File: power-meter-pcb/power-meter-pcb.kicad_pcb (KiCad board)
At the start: 2 copper layers, 3 parts, among them J1 USB4105-GF-A, U1 ESP32-S3-WROOM-1, U2 TPD3E001DRLR

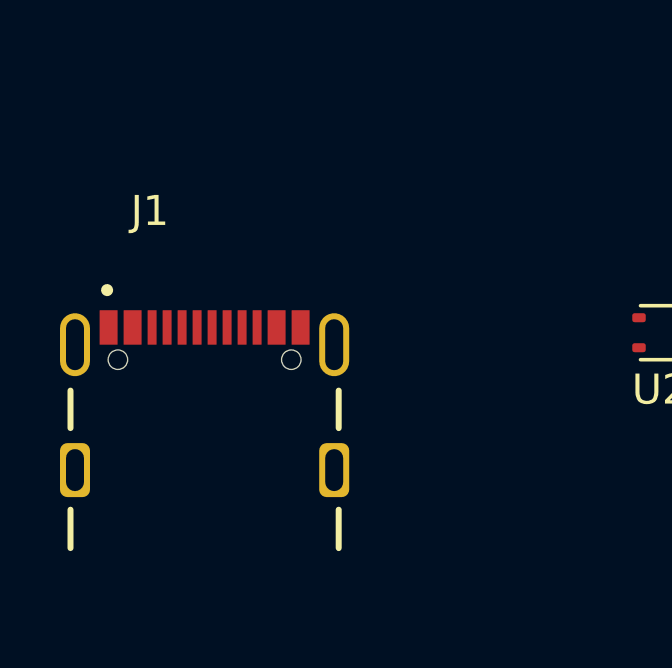
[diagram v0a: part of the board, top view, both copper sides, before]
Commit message: Added amplifier, IMU, inter board connections
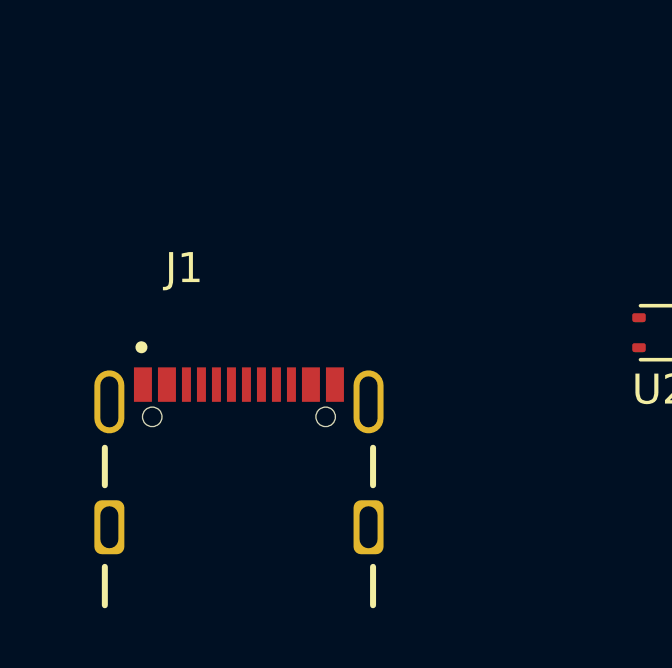
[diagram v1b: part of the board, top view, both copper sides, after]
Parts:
- moved J1 2.22 mm to (118.7, 105.4)
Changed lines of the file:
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@@
 		)
 		(fp_text user "${REFERENCE}"
-			(at 0 0 270)
+			(at 0 0 -90)
 			(layer "F.Fab")
 			(effects
@@
 	(footprint "USB4105:GCT_USB4105-GF-A"
 		(layer "F.Cu")
-		(at 117.6 103.505)
+		(at 118.745 105.41)
 		(property "Reference" "J1"
 			(at -1.825 -8.635 0)

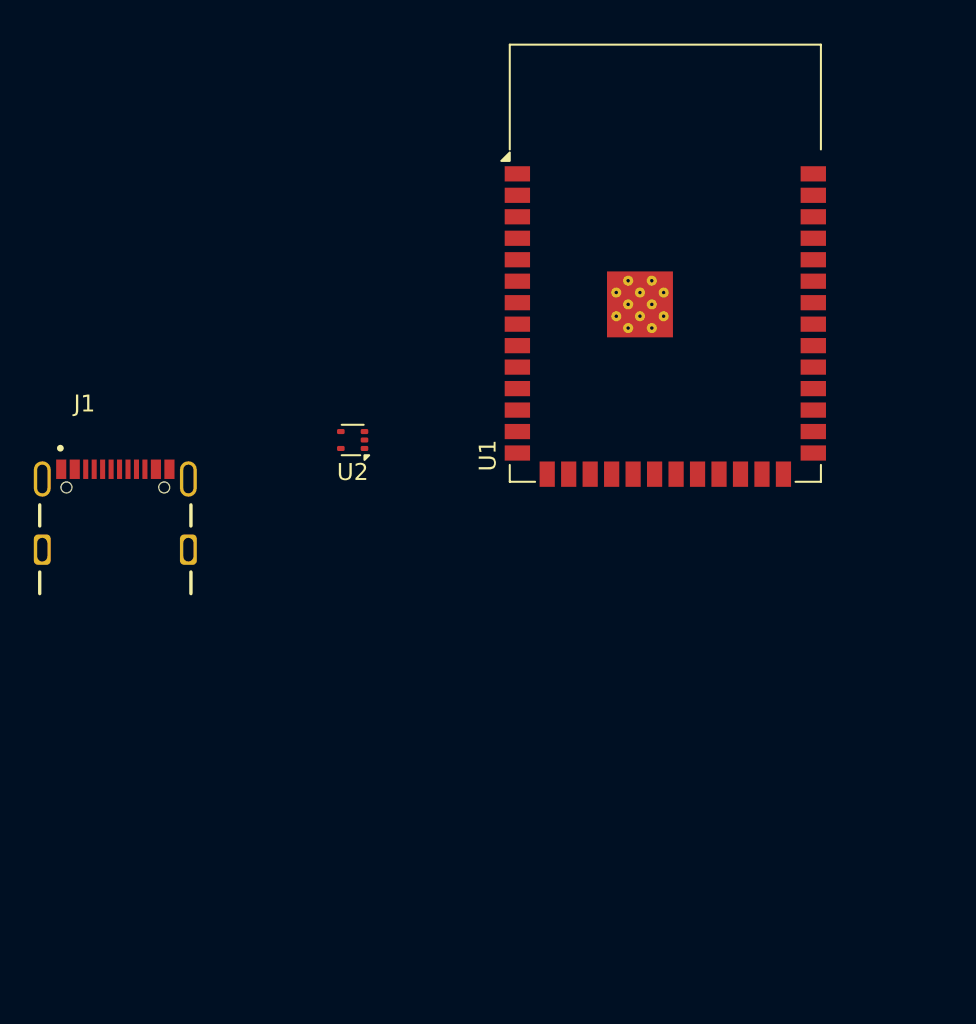
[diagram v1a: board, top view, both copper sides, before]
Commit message: Assigning footprints, extremely rough idea of size
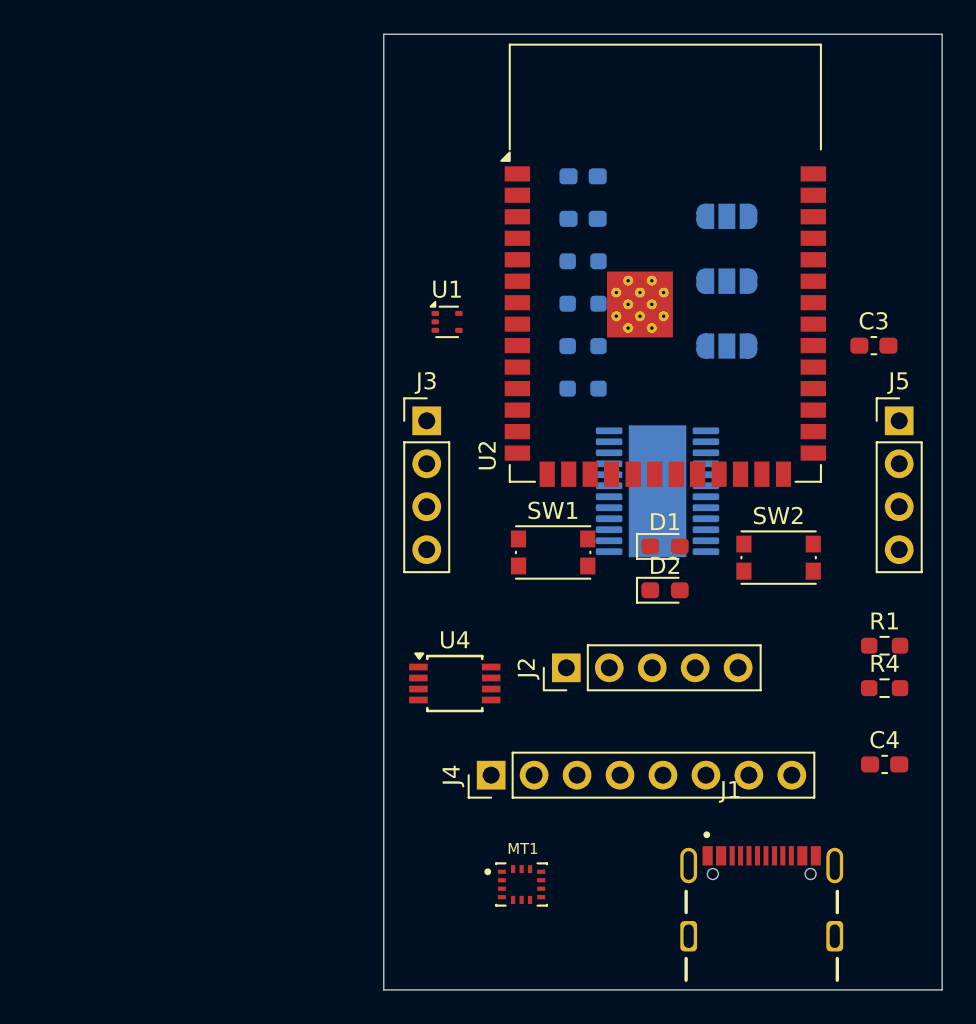
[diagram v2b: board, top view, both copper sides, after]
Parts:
- removed the U2 at (132.8, 98.9)
- added C1: 1u, Capacitor_SMD:C_0603_1608Metric_Pad1.08x0.95mm_HandSolder, B.Cu at (146.4, 83.3)
- added C2: 1u, Capacitor_SMD:C_0603_1608Metric_Pad1.08x0.95mm_HandSolder, B.Cu at (146.4, 85.8)
- added C3: C, Capacitor_SMD:C_0603_1608Metric_Pad1.08x0.95mm_HandSolder, F.Cu at (163.6, 93.3)
- added C4: 100n, Capacitor_SMD:C_0603_1608Metric_Pad1.08x0.95mm_HandSolder, F.Cu at (164.2, 118.1)
- added D1: LED, LED_SMD:LED_0603_1608Metric_Pad1.05x0.95mm_HandSolder, F.Cu at (151.3, 105.2)
- added D2: LED, LED_SMD:LED_0603_1608Metric_Pad1.05x0.95mm_HandSolder, F.Cu at (151.3, 107.8)
- added J2: Debug, Connector_PinHeader_2.54mm:PinHeader_1x05_P2.54mm_Vertical, F.Cu at (145.4, 112.4)
- added J3: Side A, Connector_PinHeader_2.54mm:PinHeader_1x04_P2.54mm_Vertical, F.Cu at (137.2, 97.8)
- added J4: Crank interconnect, Connector_PinHeader_2.54mm:PinHeader_1x08_P2.54mm_Vertical, F.Cu at (141.0, 118.7)
- added J5: Side B, Connector_PinHeader_2.54mm:PinHeader_1x04_P2.54mm_Vertical, F.Cu at (165.1, 97.8)
- added JP1: Address select, Jumper:SolderJumper-3_P1.3mm_Open_RoundedPad1.0x1.5mm, B.Cu at (154.9, 85.7)
- added JP2: Amp select, Jumper:SolderJumper-3_P1.3mm_Open_RoundedPad1.0x1.5mm, B.Cu at (154.9, 89.5)
- added JP3: Amp select, Jumper:SolderJumper-3_P1.3mm_Open_RoundedPad1.0x1.5mm, B.Cu at (154.9, 93.4)
- added MT1: ICM-42670-P, ICM-42670-P_AccelGyro:XDCR_ICM-42670-P, F.Cu at (142.8, 125.2)
- added R1: 5.1k, Resistor_SMD:R_0603_1608Metric_Pad0.98x0.95mm_HandSolder, F.Cu at (164.2, 111.1)
- added R2: 10k, Resistor_SMD:R_0603_1608Metric_Pad0.98x0.95mm_HandSolder, B.Cu at (146.4, 88.4)
- added R3: 10k, Resistor_SMD:R_0603_1608Metric_Pad0.98x0.95mm_HandSolder, B.Cu at (146.4, 90.9)
- added R4: 5.1k, Resistor_SMD:R_0603_1608Metric_Pad0.98x0.95mm_HandSolder, F.Cu at (164.2, 113.6)
- added R5: 150, Resistor_SMD:R_0603_1608Metric_Pad0.98x0.95mm_HandSolder, B.Cu at (146.4, 93.4)
- added R6: 150, Resistor_SMD:R_0603_1608Metric_Pad0.98x0.95mm_HandSolder, B.Cu at (146.4, 95.9)
- added SW1: EN, Button_Switch_SMD:SW_Push_1P1T_NO_CK_KMR2, F.Cu at (144.6, 105.6)
- added SW2: BOOT, Button_Switch_SMD:SW_Push_1P1T_NO_CK_KMR2, F.Cu at (158.0, 105.9)
- added U1: TPD3E001DRLR, Package_TO_SOT_SMD:SOT-553, F.Cu at (138.4, 91.9)
- added U3: ADS1232IPW, Package_SO:HTSSOP-24-1EP_4.4x7.8mm_P0.65mm_EP3.4x7.8mm_Mask2.4x4.68mm, B.Cu at (150.8, 102.0)
- added U4: P3T1755, Package_SO:TSSOP-8_3x3mm_P0.65mm, F.Cu at (138.8, 113.3)
- moved J1 44.5 mm to (157.0, 128.3)
- renumbered U1 to U2
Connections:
- net /DN renamed /USB and charging/USB.DN
- net /DP renamed /USB and charging/USB.DP
- J1 pad A1_B12: GND1 -> GNDD
- J1 pad B1_A12: GND1 -> GNDD
- J1 pad SH1: GND1 -> GNDD
- J1 pad SH2: GND1 -> GNDD
- J1 pad SH3: GND1 -> GNDD
- J1 pad SH4: GND1 -> GNDD
- U2 pad 1: Net-(U1-GND-Pad1) -> GNDD
- U2 pad 15: unconnected-(U1-IO3-Pad15) -> /Accelerometer/SPI.SDO
- U2 pad 16: unconnected-(U1-IO46-Pad16) -> /AMP_PWDN
- U2 pad 2: unconnected-(U1-3V3-Pad2) -> +3.3V
- U2 pad 24: unconnected-(U1-IO47-Pad24) -> /AMP2.DOUT
- U2 pad 25: unconnected-(U1-IO48-Pad25) -> /AMP2.SCLK
- U2 pad 26: unconnected-(U1-IO45-Pad26) -> /AMP1.SCLK
- U2 pad 27: unconnected-(U1-IO0-Pad27) -> /BOOT
- U2 pad 31: unconnected-(U1-IO38-Pad31) -> /LED1
- U2 pad 32: unconnected-(U1-IO39-Pad32) -> /LED2
- U2 pad 35: unconnected-(U1-IO42-Pad35) -> /AMP1.DOUT
- U2 pad 36: unconnected-(U1-RXD0-Pad36) -> /UART.RX
- U2 pad 37: unconnected-(U1-TXD0-Pad37) -> /UART.TX
- U2 pad 38: unconnected-(U1-IO2-Pad38) -> /Accelerometer/SPI.SCLK
- U2 pad 39: unconnected-(U1-IO1-Pad39) -> /Accelerometer/SPI.AC_CS
- U2 pad 4: unconnected-(U1-IO4-Pad4) -> /Accelerometer/SPI.SDI
- U2 pad 40: Net-(U1-GND-Pad1) -> GNDD
- U2 pad 41: Net-(U1-GND-Pad1) -> GNDD
- U2 pad 5: unconnected-(U1-IO5-Pad5) -> /Accelerometer/Interrupt
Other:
- board outline added: 33 x 56.5 mm

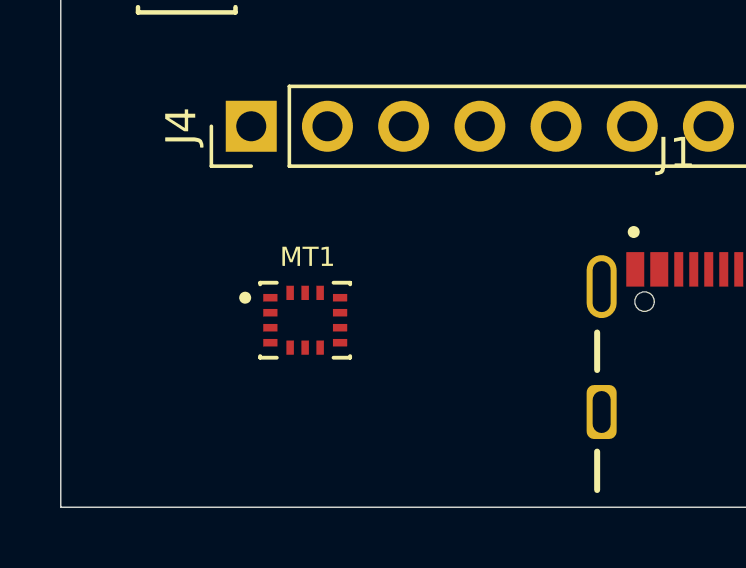
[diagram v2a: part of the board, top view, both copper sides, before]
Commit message: Added power supply to PCB
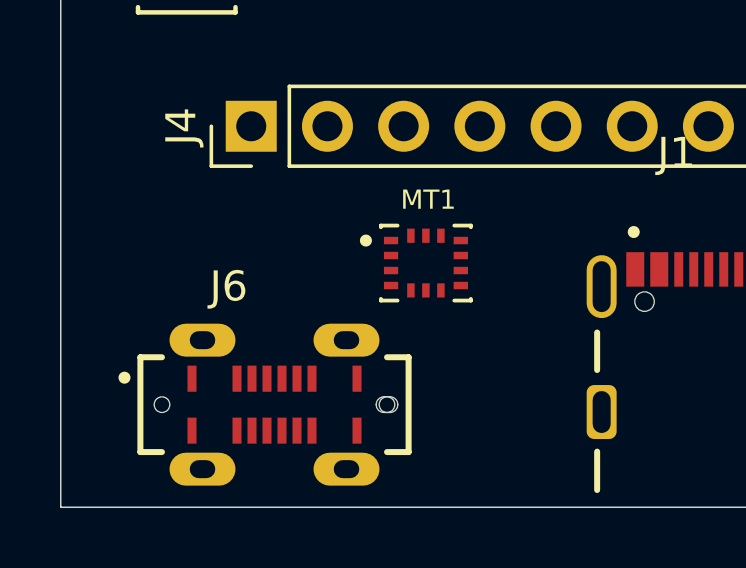
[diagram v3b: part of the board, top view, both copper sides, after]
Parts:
- added J6: USB4120-03-C_REVA, USB4120:GCT_USB4120-03-C_REVA, F.Cu at (141.7, 128.0)
- moved MT1 4.45 mm to (146.8, 123.3)
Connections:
- U4 pad 1: (no net) -> /I2C.SCL
- U4 pad 2: (no net) -> /I2C.SDA
- U4 pad 3: (no net) -> unconnected-(U4-ALERT-Pad3)
- U4 pad 4: (no net) -> GNDD
- U4 pad 5: (no net) -> GNDD
- U4 pad 6: (no net) -> GNDD
- U4 pad 7: (no net) -> Net-(JP1-C)
- U4 pad 8: (no net) -> +3.3V

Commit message: Started PCB layout
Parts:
- removed the J1 at (157.0, 128.3)
- removed the R1 at (164.2, 111.1)
- removed the R4 at (164.2, 113.6)
- added BT1: Battery_Cell, Connector_JST:JST_EH_B2B-EH-A_1x02_P2.50mm_Vertical, F.Cu at (110.5, 127.0)
- added C10: 10u, Capacitor_SMD:C_0603_1608Metric_Pad1.08x0.95mm_HandSolder, F.Cu at (109.4, 94.6)
- added C12: 0.1u, Capacitor_SMD:C_0603_1608Metric_Pad1.08x0.95mm_HandSolder, B.Cu at (138.2, 69.4)
- added C13: 0.1u, Capacitor_SMD:C_0603_1608Metric_Pad1.08x0.95mm_HandSolder, B.Cu at (128.5, 72.4)
- added C15: 0.1u, Capacitor_SMD:C_0603_1608Metric_Pad1.08x0.95mm_HandSolder, F.Cu at (112.1, 76.7)
- added C3: 10u, Capacitor_SMD:C_0603_1608Metric_Pad1.08x0.95mm_HandSolder, F.Cu at (105.1, 89.6)
- added C4: 10u, Capacitor_SMD:C_0603_1608Metric_Pad1.08x0.95mm_HandSolder, F.Cu at (105.1, 92.1)
- added C5: 0.1u, Capacitor_SMD:C_0603_1608Metric_Pad1.08x0.95mm_HandSolder, F.Cu at (105.1, 94.6)
- added C6: 10u, Capacitor_SMD:C_0603_1608Metric_Pad1.08x0.95mm_HandSolder, F.Cu at (105.1, 97.1)
- added C7: 0.1u, Capacitor_SMD:C_0603_1608Metric_Pad1.08x0.95mm_HandSolder, F.Cu at (105.1, 99.6)
- added C8: 10u, Capacitor_SMD:C_0603_1608Metric_Pad1.08x0.95mm_HandSolder, F.Cu at (109.4, 89.6)
- added C9: 10u, Capacitor_SMD:C_0603_1608Metric_Pad1.08x0.95mm_HandSolder, F.Cu at (109.4, 92.1)
- added D3: LED, LED_SMD:LED_0603_1608Metric_Pad1.05x0.95mm_HandSolder, F.Cu at (115.5, 102.2)
- added FB1: MH2029-300Y, Inductor_SMD:L_0805_2012Metric, F.Cu at (110.3, 106.6)
- added L1: 4.7uH, Inductor_SMD:L_Murata_DFE201610P, F.Cu at (115.1, 105.1)
- added NT1: NetTie_2, NetTie:NetTie-2_SMD_Pad0.5mm, B.Cu at (133.1, 70.0)
- added NT3: NetTie_2, NetTie:NetTie-2_SMD_Pad0.5mm, B.Cu at (136.7, 60.0)
- added Q1: AS2302, Package_TO_SOT_SMD:TSOT-23, F.Cu at (118.6, 90.8)
- added Q2: AS2302, Package_TO_SOT_SMD:TSOT-23, F.Cu at (116.9, 121.0)
- added Q3: AS2302, Package_TO_SOT_SMD:TSOT-23, B.Cu at (140.8, 67.2)
- added R10: 470, Resistor_SMD:R_0603_1608Metric_Pad0.98x0.95mm_HandSolder, F.Cu at (113.8, 97.1)
- added R11: 1M, Resistor_SMD:R_0603_1608Metric_Pad0.98x0.95mm_HandSolder, F.Cu at (115.1, 73.7)
- added R12: 1M, Resistor_SMD:R_0603_1608Metric_Pad0.98x0.95mm_HandSolder, F.Cu at (121.8, 79.2)
- added R13: 47, Resistor_SMD:R_0603_1608Metric_Pad0.98x0.95mm_HandSolder, B.Cu at (139.1, 75.1)
- added R14: 47, Resistor_SMD:R_0603_1608Metric_Pad0.98x0.95mm_HandSolder, B.Cu at (139.1, 73.6)
- added R15: 47, Resistor_SMD:R_0603_1608Metric_Pad0.98x0.95mm_HandSolder, B.Cu at (139.1, 72.1)
- added R5: 5.1k, Resistor_SMD:R_0603_1608Metric_Pad0.98x0.95mm_HandSolder, F.Cu at (109.4, 97.1)
- added R6: 2.2k, Resistor_SMD:R_0603_1608Metric_Pad0.98x0.95mm_HandSolder, F.Cu at (109.4, 99.6)
- added R7: 470, Resistor_SMD:R_0603_1608Metric_Pad0.98x0.95mm_HandSolder, F.Cu at (113.8, 89.6)
- added R8: 5.1k, Resistor_SMD:R_0603_1608Metric_Pad0.98x0.95mm_HandSolder, F.Cu at (113.8, 92.1)
- added R9: 2k, Resistor_SMD:R_0603_1608Metric_Pad0.98x0.95mm_HandSolder, F.Cu at (113.8, 94.6)
- added U3: MCP73831-2-OT, Package_TO_SOT_SMD:SOT-23-5, F.Cu at (105.5, 103.3)
- added U5: S-8261AAJMD-G2JT2U, Package_TO_SOT_SMD:SOT-23-6, F.Cu at (105.5, 107.9)
- added U6: TPS63031DSK, Package_SON:WSON-10-1EP_2.5x2.5mm_P0.5mm_EP1.2x2mm, F.Cu at (123.2, 103.2)
- C1, C2: moved to F.Cu
- C11: renamed from C3; value C -> 0.1u; moved to B.Cu
- C14: renamed from C4; value 100n -> 0.1u
- J4: renamed from J3; moved to B.Cu
- J5: moved to B.Cu
- JP3: renamed from JP1; moved to F.Cu
- R1: renamed from R2; moved to F.Cu
- R2: renamed from R3; moved to F.Cu
- R3: renamed from R5; moved to F.Cu
- R4: renamed from R6; moved to F.Cu
- U7: renamed from U3; footprint Package_SO:HTSSOP-24-1EP_4.4x7.8mm_P0.65mm_EP3.4x7.8mm_Mask2.4x4.68mm -> Package_SO:TSSOP-24_4.4x7.8mm_P0.65mm
- moved MT1 47.3 mm to (155.0, 76.7)
- moved C11 44.0 mm to (128.5, 66.8), turned to 90 degrees
- moved J5 42.7 mm to (147.3, 58.9), turned to 180 degrees
- moved J4 41.3 mm to (123.2, 58.9), turned to 180 degrees
- moved U7 36.8 mm to (133.3, 69.6), turned to 0 degrees
- moved J2 36.1 mm to (129.0, 80.2)
- moved U1 36.1 mm to (135.3, 56.1)
- moved JP3 36.0 mm to (170.7, 53.3), turned to 90 degrees
- moved JP2 24.5 mm to (143.8, 71.5), turned to 90 degrees
- moved JP1 17.1 mm to (143.8, 76.6), turned to 90 degrees
- moved R2 9.35 mm to (155.6, 88.9), turned to 0 degrees
- moved R3 7.63 mm to (154.0, 93.0), turned to 0 degrees
- moved R4 7.59 mm to (153.8, 97.5), turned to 0 degrees
- moved R1 6.13 mm to (146.4, 94.5), turned to 0 degrees
- moved C2 4.60 mm to (146.8, 90.4), turned to 0 degrees
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- renumbered J4 to J1, J6 to J3, JP2 to JP1, JP3 to JP2, U2 to U1, U4 to U2, U1 to U4
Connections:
- net Net-(J3-Pin_2) renamed /Strain gauge amplifier/GA
- net Net-(J3-Pin_3) renamed /Strain gauge amplifier/GB
- J3 pad A1: unconnected-(J6-GND_A-PadA1) -> GNDD
- J3 pad A12: unconnected-(J6-GND_A__1-PadA12) -> GNDD
- J3 pad A4: unconnected-(J6-VBUS_A-PadA4) -> +5V
- J3 pad A5: unconnected-(J6-CC1-PadA5) -> Net-(J3-CC1)
- J3 pad A6: unconnected-(J6-D1+-PadA6) -> /USB and charging/USB.DP
- J3 pad A7: unconnected-(J6-D1--PadA7) -> /USB and charging/USB.DN
- J3 pad A9: unconnected-(J6-VBUS_A__1-PadA9) -> +5V
- J3 pad B1: unconnected-(J6-GND_B-PadB1) -> GNDD
- J3 pad B12: unconnected-(J6-GND_B__1-PadB12) -> GNDD
- J3 pad B4: unconnected-(J6-VBUS_B-PadB4) -> +5V
- J3 pad B5: unconnected-(J6-CC2-PadB5) -> Net-(J3-CC2)
- J3 pad B6: unconnected-(J6-D2+-PadB6) -> /USB and charging/USB.DN
- J3 pad B7: unconnected-(J6-D2--PadB7) -> /USB and charging/USB.DP
- J3 pad B9: unconnected-(J6-VBUS_B__1-PadB9) -> +5V
- J3 pad S1: unconnected-(J6-SHIELD-PadS1) -> GNDD
- J3 pad S2: unconnected-(J6-SHIELD__1-PadS2) -> GNDD
- J3 pad S3: unconnected-(J6-SHIELD__2-PadS3) -> GNDD
- J3 pad S4: unconnected-(J6-SHIELD__3-PadS4) -> GNDD
- J4 pad 4: GNDA -> /Strain gauge amplifier/GN
- J5 pad 4: GNDA -> /Strain gauge amplifier/GN
- U1 pad 11: unconnected-(U2-IO18-Pad11) -> /USB and charging/Battery voltage
- U1 pad 23: unconnected-(U2-IO21-Pad23) -> /USB and charging/Power save
- U7 pad 15: GNDA -> /Strain gauge amplifier/GN
- U7 pad 16: +3.3VA -> /Strain gauge amplifier/GP
- U7 pad 22: /AMP_PWDN -> Net-(U7-~{PWDN})
- U7 pad 23: /AMP.SCLK -> Net-(U7-SCLK)
- U7 pad 24: /AMP.DOUT -> Net-(U7-~{DRDY}/DOUT)
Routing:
- net /Strain gauge amplifier/GN: track 0.00 -> 39.4 mm
- net /Strain gauge amplifier/GA: track 0.00 -> 31.0 mm, vias 0 -> 3
- net /Strain gauge amplifier/GB: track 0.00 -> 30.5 mm, vias 0 -> 2
- net +3.3VA: track 0.00 -> 28.2 mm
- net GNDA: track 0.00 -> 10.4 mm
- net GNDD: track 0.00 -> 10.1 mm
- net +3.3V: track 0.00 -> 9.76 mm
- net /AMP_PWDN: track 0.00 -> 4.27 mm
- net Net-(U7-~{DRDY}/DOUT): track 0.00 -> 2.82 mm
- net Net-(C11-Pad2): track 0.00 -> 2.60 mm
- net Net-(U7-SCLK): track 0.00 -> 2.46 mm
- net Net-(U7-~{PWDN}): track 0.00 -> 2.10 mm
- net Net-(C11-Pad1): track 0.00 -> 2.02 mm
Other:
- board size 33 x 56.5 mm -> 0.7 x 0.5 mm
